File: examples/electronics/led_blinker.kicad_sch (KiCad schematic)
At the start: 3 parts, among them J1 JST-PH-2

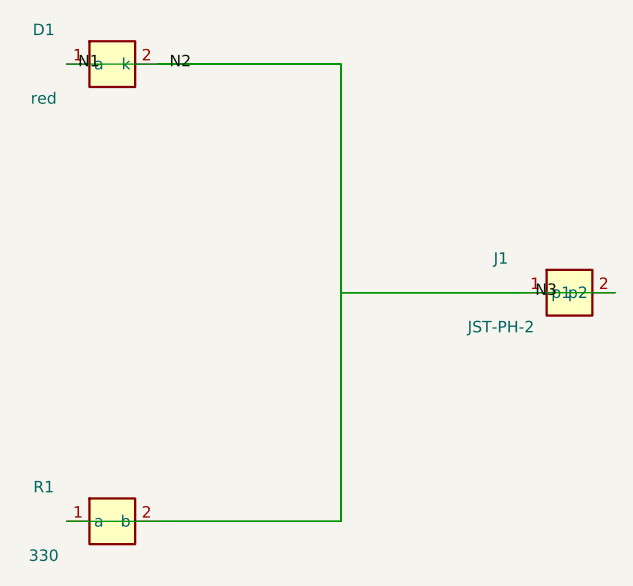
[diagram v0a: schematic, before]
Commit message: feat(electronics): power ratings — proven P = V × I per part (B5)
Clause surface: rating 0.25; (max watts) | rating any; (declared
unrated) — uniform on type/obj/cell bodies, mirroring tolerance
(Rating::Watts/Any in ast::top, at_rating_clause/parse_rating_clause
shared helpers, wired into both clause loops).

Proving: after the current fixpoint, every valued two-pin part with
BOTH endpoints voltage-classed has PROVEN dissipation P = dV²/R:
- above the rating -> violation naming part, type, value, derived P;
- no clause -> undeclared-decision violation (same forced-explicitness
  doctrine as tolerance);
- within -> proof fact ('P(r1) = 32.6 mW <= 250.0 mW rating').
One-sided parts have no proven dV — nothing forced (LED demo stays
non-ohmic, its series resistor unclassable without a ground drive).
Zero-drop parts (straps) force nothing.

Fixtures rated (divider + kirchhoff types; divider board now also
asserts violation-free). 3 new tests: above-rating violates,
missing-rating undeclared, zero-drop needs nothing.

build.rs: create target/compiler-in-briv — fresh-worktree bootstrap
was silently failing the gpu-rt RT compile (bin link: undefined
briev_accel_*). 2160 green, exit 0; demo emits.
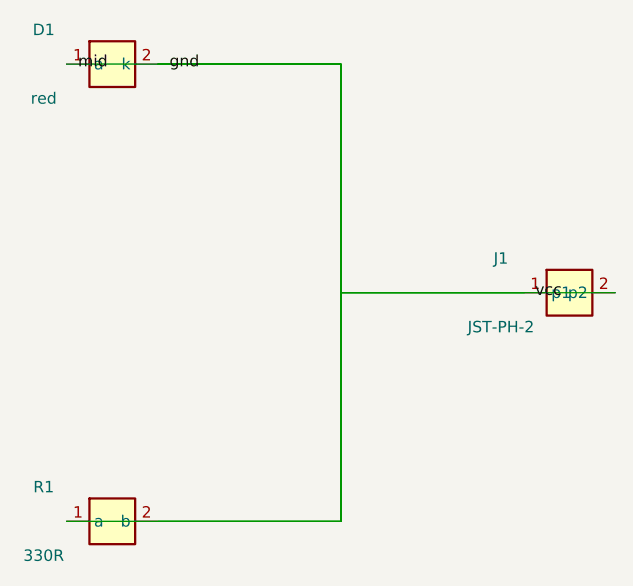
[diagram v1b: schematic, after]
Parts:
- R1: value 330 -> 330R
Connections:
- net N1 renamed gnd
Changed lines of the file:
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@@
     (in_bom yes) (on_board yes)
     (property "Reference" "R1" (at 93.98 97.79 0) (effects (font (size 1.27 1.27))))
-    (property "Value" "330" (at 93.98 105.41 0) (effects (font (size 1.27 1.27))))
+    (property "Value" "330R" (at 93.98 105.41 0) (effects (font (size 1.27 1.27))))
     (property "Footprint" "0805" (at 101.60 101.60 0) (effects (font (size 1.27 1.27)) (hide yes)))
     (instances (project briev
@@
   (wire (pts (xy 127.00 50.80) (xy 127.00 101.60)) (stroke (width 0) (type default)))
   (wire (pts (xy 127.00 101.60) (xy 106.68 101.60)) (stroke (width 0) (type default)))
-  (label "N1" (at 97.79 50.80 0) (effects (font (size 1.27 1.27)) (justify (left bottom))))
+  (label "mid" (at 97.79 50.80 0) (effects (font (size 1.27 1.27)) (justify (left bottom))))
   (wire (pts (xy 106.68 50.80) (xy 127.00 50.80)) (stroke (width 0) (type default)))
   (wire (pts (xy 127.00 50.80) (xy 127.00 76.20)) (stroke (width 0) (type default)))
   (wire (pts (xy 127.00 76.20) (xy 157.48 76.20)) (stroke (width 0) (type default)))
-  (label "N2" (at 107.95 50.80 0) (effects (font (size 1.27 1.27)) (justify (left bottom))))
+  (label "gnd" (at 107.95 50.80 0) (effects (font (size 1.27 1.27)) (justify (left bottom))))
   (wire (pts (xy 147.32 76.20) (xy 127.00 76.20)) (stroke (width 0) (type default)))
   (wire (pts (xy 127.00 76.20) (xy 127.00 101.60)) (stroke (width 0) (type default)))
   (wire (pts (xy 127.00 101.60) (xy 96.52 101.60)) (stroke (width 0) (type default)))
-  (label "N3" (at 148.59 76.20 0) (effects (font (size 1.27 1.27)) (justify (left bottom))))
+  (label "vcc" (at 148.59 76.20 0) (effects (font (size 1.27 1.27)) (justify (left bottom))))
 )

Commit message: feat(electronics): E14a gate fixture — pin intents, prefix refs, prelude class injection (Slices 2-5)
usb_sensor.ebv (§3.2 gate) compiles to a kicad_sch; error matrix
(4 negatives), determinism, and E10 hygiene tests land. General
fixes, none fixture-shaped:

- prelude-electronics injects std/electronics.bv into import-less
  sources (class ascriptions previously resolved to not-in-scope
  defaults: can_drive false)
- resolve_pin: bare indexed pins (u2.gpio[0]) + shared lookup_pin
- pin-level drive intents (inst.pin = true;) — FactSink form check,
  D13 completion; previously a silent drop
- typechecker: declarative-intent admission + instance-array base
  name binding
- reference designators per prefix (duplicate refs were invalid KiCad)
- decoupling is a present-state obligation (unpop caps excluded)

Ledger E1/E10 closed; design record E14a gate-passed with delta list;
new open gap: derive-on-type clauses.
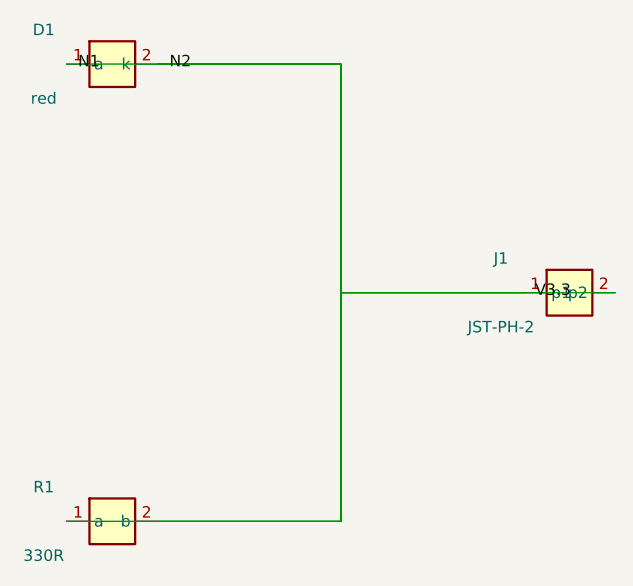
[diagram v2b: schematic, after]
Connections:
- net gnd renamed N1
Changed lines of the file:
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@@
   (wire (pts (xy 127.00 50.80) (xy 127.00 101.60)) (stroke (width 0) (type default)))
   (wire (pts (xy 127.00 101.60) (xy 106.68 101.60)) (stroke (width 0) (type default)))
-  (label "mid" (at 97.79 50.80 0) (effects (font (size 1.27 1.27)) (justify (left bottom))))
+  (label "N1" (at 97.79 50.80 0) (effects (font (size 1.27 1.27)) (justify (left bottom))))
   (wire (pts (xy 106.68 50.80) (xy 127.00 50.80)) (stroke (width 0) (type default)))
   (wire (pts (xy 127.00 50.80) (xy 127.00 76.20)) (stroke (width 0) (type default)))
   (wire (pts (xy 127.00 76.20) (xy 157.48 76.20)) (stroke (width 0) (type default)))
-  (label "gnd" (at 107.95 50.80 0) (effects (font (size 1.27 1.27)) (justify (left bottom))))
+  (label "N2" (at 107.95 50.80 0) (effects (font (size 1.27 1.27)) (justify (left bottom))))
   (wire (pts (xy 147.32 76.20) (xy 127.00 76.20)) (stroke (width 0) (type default)))
   (wire (pts (xy 127.00 76.20) (xy 127.00 101.60)) (stroke (width 0) (type default)))
   (wire (pts (xy 127.00 101.60) (xy 96.52 101.60)) (stroke (width 0) (type default)))
-  (label "vcc" (at 148.59 76.20 0) (effects (font (size 1.27 1.27)) (justify (left bottom))))
+  (label "V3.3" (at 148.59 76.20 0) (effects (font (size 1.27 1.27)) (justify (left bottom))))
 )

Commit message: feat(electronics): component laws Slice 5 — stdlib laws and fixtures
Add generic dimensioned law parameters on pin-bearing component types
(spec ForwardVoltage: Volt; spec DynamicResistance: Ohm;), including
type-level quantity defaults. Unknown spec names remain rejected outside
component bodies.

- stdlib Resistor and Wire declare always-active laws
- stdlib Diode and Led declare forward/reverse piecewise laws
- later component declarations shadow prelude declarations, so local
  same-named types cannot inherit stdlib laws by accident
- migrate led_blinker to stdlib laws and structured datasheet physics;
  the solver proves its 4.4 mA operating point
- migrate usb_sensor resistance values to structured specs; keep its
  local Resistor law-free until SPST conditional-topology state exists
- document the law mechanism and remaining fixture migration boundary

Full lib suite green; Praetor no new diagnostics; both fixtures emit.
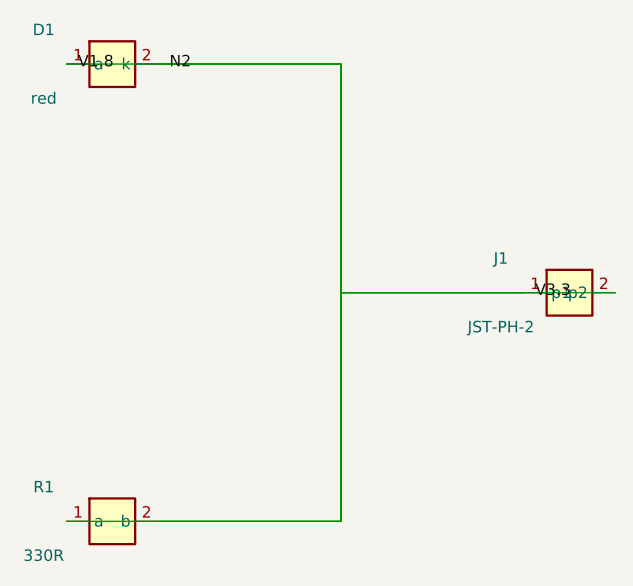
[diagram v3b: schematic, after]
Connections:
- net N1 renamed N2
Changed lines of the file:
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@@
   (wire (pts (xy 127.00 50.80) (xy 127.00 101.60)) (stroke (width 0) (type default)))
   (wire (pts (xy 127.00 101.60) (xy 106.68 101.60)) (stroke (width 0) (type default)))
-  (label "N1" (at 97.79 50.80 0) (effects (font (size 1.27 1.27)) (justify (left bottom))))
+  (label "V1.8" (at 97.79 50.80 0) (effects (font (size 1.27 1.27)) (justify (left bottom))))
   (wire (pts (xy 106.68 50.80) (xy 127.00 50.80)) (stroke (width 0) (type default)))
   (wire (pts (xy 127.00 50.80) (xy 127.00 76.20)) (stroke (width 0) (type default)))

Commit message: electronics: emitted sheets load in KiCad 10 (E3 prep)
Four load blockers, each alone a refusal (found by section-bisection
against kicad-cli 10.0.6):
- uuid last group {:012} decimal (up to 15 digits) -> {:012x}
- label justify (justify (left bottom)) -> bare (justify left bottom)
- missing mandatory (sheet_instances (path "/" (page "1")))
- power-symbol Reference property `hide yes` -> bare `hide`
  (nested (hide yes) inside effects stays legal)

Structural tests: emitted_sheet_is_kicad_10_loadable (existing) +
power_symbol_hide_is_bare (new). Fixture gate: kicad-cli sch erc now
loads all 5 emitted fixtures; led_blinker/operating_states/
data_table_tile are ERC-error-clean. usb_sensor (5) and spst_modes (1)
carry real electrical ERC defects — tracked OPEN in BUGS.md as the
E3 follow-up, not loadability.

Regenerated the stale led_blinker.kicad_sch (carried the decimal uuids).
cargo test --lib: 2731/0.
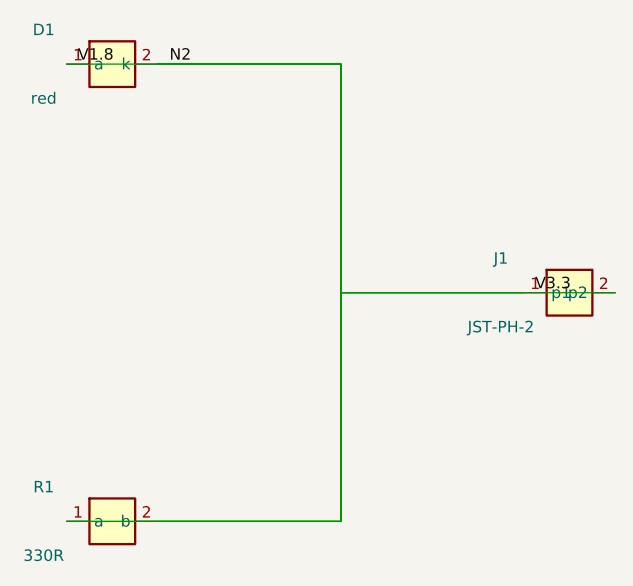
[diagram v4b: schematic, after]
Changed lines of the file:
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@@
     (property "Footprint" "0805" (at 101.60 50.80 0) (effects (font (size 1.27 1.27)) (hide yes)))
     (instances (project briev
-      (path "/b713e5c0-0000-4000-8000-108940779875558" (reference "D1") (unit 1))
+      (path "/b713e5c0-0000-4000-8000-6314c07c6ce6" (reference "D1") (unit 1))
     ))
   )
@@
     (property "Footprint" "JST-PH" (at 152.40 76.20 0) (effects (font (size 1.27 1.27)) (hide yes)))
     (instances (project briev
-      (path "/b713e5c0-0000-4000-8000-108940779875558" (reference "J1") (unit 1))
+      (path "/b713e5c0-0000-4000-8000-6314c07c6ce6" (reference "J1") (unit 1))
     ))
   )
@@
     (property "Footprint" "0805" (at 101.60 101.60 0) (effects (font (size 1.27 1.27)) (hide yes)))
     (instances (project briev
-      (path "/b713e5c0-0000-4000-8000-108940779875558" (reference "R1") (unit 1))
+      (path "/b713e5c0-0000-4000-8000-6314c07c6ce6" (reference "R1") (unit 1))
     ))
   )
@@
   (wire (pts (xy 127.00 50.80) (xy 127.00 101.60)) (stroke (width 0) (type default)))
   (wire (pts (xy 127.00 101.60) (xy 106.68 101.60)) (stroke (width 0) (type default)))
-  (label "V1.8" (at 97.79 50.80 0) (effects (font (size 1.27 1.27)) (justify (left bottom))))
+  (label "V1.8" (at 97.79 50.80 0) (effects (font (size 1.27 1.27)) (justify left bottom)))
   (wire (pts (xy 106.68 50.80) (xy 127.00 50.80)) (stroke (width 0) (type default)))
   (wire (pts (xy 127.00 50.80) (xy 127.00 76.20)) (stroke (width 0) (type default)))
   (wire (pts (xy 127.00 76.20) (xy 157.48 76.20)) (stroke (width 0) (type default)))
-  (label "N2" (at 107.95 50.80 0) (effects (font (size 1.27 1.27)) (justify (left bottom))))
+  (label "N2" (at 107.95 50.80 0) (effects (font (size 1.27 1.27)) (justify left bottom)))
   (wire (pts (xy 147.32 76.20) (xy 127.00 76.20)) (stroke (width 0) (type default)))
   (wire (pts (xy 127.00 76.20) (xy 127.00 101.60)) (stroke (width 0) (type default)))
   (wire (pts (xy 127.00 101.60) (xy 96.52 101.60)) (stroke (width 0) (type default)))
-  (label "V3.3" (at 148.59 76.20 0) (effects (font (size 1.27 1.27)) (justify (left bottom))))
+  (label "V3.3" (at 148.59 76.20 0) (effects (font (size 1.27 1.27)) (justify left bottom)))
+  (sheet_instances
+    (path "/" (page "1"))
+  )
 )
